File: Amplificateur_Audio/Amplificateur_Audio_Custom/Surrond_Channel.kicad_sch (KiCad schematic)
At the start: 84 parts, among them J401 Surrond Left+, J405 Analog input Connector, U401 PCM5252RHBR, U402 TPA3244DDWR, U403 74LVC1G125, U404 74LVC1G125

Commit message: Ajout de l'assignation des compostants et des empreintes jusqu'à la page 6
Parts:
- C401, C403, C405, C413, C415, C417, C419, C426, C427, C428, C429, C430, C431, C434, C435, C437, C439, C442, C443, C444, C445, C446: footprint (none) -> Capacitor_SMD:C_0603_1608Metric_Pad1.08x0.95mm_HandSolder
- C402, C404, C406, C407, C408, C409, C410, C411, C432, C433: footprint (none) -> Capacitor_SMD:C_0402_1005Metric_Pad0.74x0.62mm_HandSolder
- C412, C414, C416, C418, C420, C421, C422, C423, C424, C425: footprint (none) -> Capacitor_SMD:C_1206_3216Metric_Pad1.33x1.80mm_HandSolder
- C436, C438, C440, C441: footprint (none) -> Capacitor_SMD:C_1210_3225Metric_Pad1.33x2.70mm_HandSolder
- J401, J402, J403, J404: footprint (none) -> NewLibrary:630661MouserReel
- J405: footprint (none) -> Connector_PinHeader_2.54mm:PinHeader_2x25_P2.54mm_Vertical_SMD
- JP401, JP402, JP403, JP404: footprint (none) -> Connector_PinHeader_2.54mm:PinHeader_1x03_P2.54mm_Vertical_SMD_Pin1Left
- L401: footprint (none) -> Inductor_SMD:L_0603_1608Metric_Pad1.05x0.95mm_HandSolder
- L402, L403: footprint (none) -> NewLibrary:UA8014ALD
- R401, R402, R403, R404, R405, R406, R407: footprint (none) -> Resistor_SMD:R_0402_1005Metric_Pad0.72x0.64mm_HandSolder
- R408, R409, R410, R411, R412, R413, R414, R415, R416, R417, R419, R420, R421, R422: footprint (none) -> Resistor_SMD:R_0603_1608Metric_Pad0.98x0.95mm_HandSolder
- R418: footprint (none) -> Resistor_SMD:R_0201_0603Metric_Pad0.64x0.40mm_HandSolder
- U401: footprint (none) -> Package_DFN_QFN:Texas_RHB0032E_VQFN-32-1EP_5x5mm_P0.5mm_EP3.45x3.45mm_ThermalVias
- U403, U404: footprint (none) -> Package_TO_SOT_SMD:SOT-353_SC-70-5_Handsoldering
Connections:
- net 12V: now also C428.2; no longer C427.2
- net 3.3V-4: now also C403.2; no longer C405.2
- net GND: now also C430.2; no longer C430.1
- net VDD1: now also C427.2; no longer C428.2
- net at C404.2, R408.1, U401.14 (AVDD): now also C405.2; no longer C403.2
- net at U402.9 (AVDD): now also C430.1; no longer C430.2

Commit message: Ajout de point de test et début du routage
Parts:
- C422, C425: footprint Capacitor_SMD:C_1206_3216Metric_Pad1.33x1.80mm_HandSolder -> Capacitor_SMD:CP_Elec_16x17.5
- J402: value ~ -> Surrond Left-
- J403: value ~ -> Surrond Right+
- J404: value ~ -> SurroundRight-
- R418: footprint Resistor_SMD:R_0201_0603Metric_Pad0.64x0.40mm_HandSolder -> Resistor_SMD:R_0603_1608Metric_Pad0.98x0.95mm_HandSolder
- U402: footprint DDV0044D_N -> NewLibrary:DDV0044D_N
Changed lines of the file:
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@@
 	)
 	(symbol
+		(lib_id "Device:C_Polarized_Small_US")
+		(at 297.18 46.355 0)
+		(unit 1)
+		(exclude_from_sim no)
+		(in_bom yes)
+		(on_board yes)
+		(dnp no)
+		(fields_autoplaced yes)
+		(property "Reference" "C425"
+			(at 299.72 44.6531 0)
+			(effects
+				(font
+					(size 1.27 1.27)
+				)
+				(justify left)
+			)
+		)
+		(property "Value" "1000uF"
+			(at 299.72 47.1931 0)
+			(effects
+				(font
+					(size 1.27 1.27)
+				)
+				(justify left)
+			)
+		)
+		(property "Footprint" "Capacitor_SMD:CP_Elec_16x17.5"
+			(at 297.18 46.355 0)
+			(effects
+				(font
+					(size 1.27 1.27)
+				)
+				(hide yes)
+			)
+		)
+		(property "Datasheet" "~"
+			(at 297.18 46.355 0)
+			(effects
+				(font
+					(size 1.27 1.27)
+				)
+				(hide yes)
+			)
+		)
+		(property "Description" "EEV-FK1H102M"
+			(at 297.18 46.355 0)
+			(effects
+				(font
+					(size 1.27 1.27)
+				)
+				(hide yes)
+			)
+		)
+		(pin "1"
+		)
+		(pin "2"
+		)
+		(instances
+			(project "Amplificateur_Audio"
+				(path "/bf9cc67f-178f-4c8c-b6a6-249a1896d599/2266f535-6438-4aa9-912a-4ebf19d1b357"
+					(reference "C425")
+					(unit 1)
+				)
+			)
+		)
+	)
+	(symbol
 		(lib_id "Device:C_Small")
 		(at 262.89 178.435 90)
@@
 	)
 	(symbol
-		(lib_id "Device:C_Polarized_Small_US")
-		(at 297.18 46.355 0)
-		(unit 1)
-		(exclude_from_sim no)
-		(in_bom yes)
-		(on_board yes)
-		(dnp no)
-		(fields_autoplaced yes)
-		(property "Reference" "C425"
-			(at 299.72 44.6531 0)
-			(effects
-				(font
-					(size 1.27 1.27)
-				)
-				(justify left)
-			)
-		)
-		(property "Value" "1000uF"
-			(at 299.72 47.1931 0)
-			(effects
-				(font
-					(size 1.27 1.27)
-				)
-				(justify left)
-			)
-		)
-		(property "Footprint" "Capacitor_SMD:C_1206_3216Metric_Pad1.33x1.80mm_HandSolder"
-			(at 297.18 46.355 0)
-			(effects
-				(font
-					(size 1.27 1.27)
-				)
-				(hide yes)
-			)
-		)
-		(property "Datasheet" "~"
-			(at 297.18 46.355 0)
-			(effects
-				(font
-					(size 1.27 1.27)
-				)
-				(hide yes)
-			)
-		)
-		(property "Description" "GRM31MR71H105KA88L"
-			(at 297.18 46.355 0)
-			(effects
-				(font
-					(size 1.27 1.27)
-				)
-				(hide yes)
-			)
-		)
-		(pin "1"
-		)
-		(pin "2"
-		)
-		(instances
-			(project "Amplificateur_Audio"
-				(path "/bf9cc67f-178f-4c8c-b6a6-249a1896d599/2266f535-6438-4aa9-912a-4ebf19d1b357"
-					(reference "C425")
-					(unit 1)
-				)
-			)
-		)
-	)
-	(symbol
 		(lib_id "Device:C_Small")
 		(at 31.75 41.275 180)
@@
 			)
 		)
-		(property "Footprint" "DDV0044D_N"
+		(property "Footprint" "NewLibrary:DDV0044D_N"
 			(at 295.91 135.255 0)
 			(effects
@@
 			)
 		)
-		(property "Value" "~"
+		(property "Value" "Surrond Right+"
 			(at 401.955 109.22 0)
 			(effects
@@
 					(size 1.27 1.27)
 				)
+				(hide yes)
 			)
 		)
@@
 			)
 		)
-		(property "Value" "~"
+		(property "Value" "SurroundRight-"
 			(at 402.59 130.81 0)
 			(effects
@@
 					(size 1.27 1.27)
 				)
+				(hide yes)
 			)
 		)
@@
 	)
 	(symbol
-		(lib_id "Device:C_Small")
-		(at 184.15 69.215 90)
-		(unit 1)
-		(exclude_from_sim no)
-		(in_bom yes)
-		(on_board no)
-		(dnp no)
-		(property "Reference" "C414"
-			(at 184.023 64.262 90)
-			(effects
-				(font
-					(size 1.27 1.27)
-				)
-			)
-		)
-		(property "Value" "10uF"
-			(at 184.404 65.913 90)
-			(effects
-				(font
-					(size 1.27 1.27)
-				)
-			)
-		)
-		(property "Footprint" "Capacitor_SMD:C_1206_3216Metric_Pad1.33x1.80mm_HandSolder"
-			(at 184.15 69.215 0)
-			(effects
-				(font
-					(size 1.27 1.27)
-				)
-				(hide yes)
-			)
-		)
-		(property "Datasheet" "~"
-			(at 184.15 69.215 0)
-			(effects
-				(font
-					(size 1.27 1.27)
-				)
-				(hide yes)
-			)
-		)
-		(property "Description" "GRM31CR71C106KAC7L"
-			(at 184.15 69.215 0)
-			(effects
-				(font
-					(size 1.27 1.27)
-				)
-				(hide yes)
-			)
-		)
-		(pin "2"
-		)
-		(pin "1"
-		)
-		(instances
-			(project "BarreDeSonTI"
-				(path "/bf9cc67f-178f-4c8c-b6a6-249a1896d599/2266f535-6438-4aa9-912a-4ebf19d1b357"
-					(reference "C414")
-					(unit 1)
-				)
-			)
-		)
-	)
-	(symbol
 		(lib_id "power:Earth")
 		(at 337.82 169.545 0)
@@
 			)
 		)
-		(property "Value" "~"
+		(property "Value" "Surrond Left-"
 			(at 401.955 86.36 0)
 			(effects
@@
 					(size 1.27 1.27)
 				)
+				(hide yes)
 			)
 		)
@@
 	(symbol
 		(lib_id "Device:C_Small")
+		(at 184.15 69.215 90)
+		(unit 1)
+		(exclude_from_sim no)
+		(in_bom yes)
+		(on_board yes)
+		(dnp no)
+		(property "Reference" "C414"
+			(at 184.023 64.262 90)
+			(effects
+				(font
+					(size 1.27 1.27)
+				)
+			)
+		)
+		(property "Value" "10uF"
+			(at 184.404 65.913 90)
+			(effects
+				(font
+					(size 1.27 1.27)
+				)
+			)
+		)
+		(property "Footprint" "Capacitor_SMD:C_1206_3216Metric_Pad1.33x1.80mm_HandSolder"
+			(at 184.15 69.215 0)
+			(effects
+				(font
+					(size 1.27 1.27)
+				)
+				(hide yes)
+			)
+		)
+		(property "Datasheet" "~"
+			(at 184.15 69.215 0)
+			(effects
+				(font
+					(size 1.27 1.27)
+				)
+				(hide yes)
+			)
+		)
+		(property "Description" "GRM31CR71C106KAC7L"
+			(at 184.15 69.215 0)
+			(effects
+				(font
+					(size 1.27 1.27)
+				)
+				(hide yes)
+			)
+		)
+		(pin "2"
+		)
+		(pin "1"
+		)
+		(instances
+			(project "Amplificateur_Audio"
+				(path "/bf9cc67f-178f-4c8c-b6a6-249a1896d599/2266f535-6438-4aa9-912a-4ebf19d1b357"
+					(reference "C414")
+					(unit 1)
+				)
+			)
+		)
+	)
+	(symbol
+		(lib_id "Device:C_Small")
 		(at 370.205 92.075 180)
 		(unit 1)
@@
 			)
 		)
-		(property "Footprint" "Resistor_SMD:R_0201_0603Metric_Pad0.64x0.40mm_HandSolder"
+		(property "Footprint" "Resistor_SMD:R_0603_1608Metric_Pad0.98x0.95mm_HandSolder"
 			(at 266.7 198.755 0)
 			(effects
@@
 			)
 		)
-		(property "Footprint" "Capacitor_SMD:C_1206_3216Metric_Pad1.33x1.80mm_HandSolder"
+		(property "Footprint" "Capacitor_SMD:CP_Elec_16x17.5"
 			(at 290.83 27.305 0)
 			(effects
@@
 			)
 		)
-		(property "Description" "GRM31MR71H105KA88L"
+		(property "Description" "EEV-FK1H102M"
 			(at 290.83 27.305 0)
 			(effects

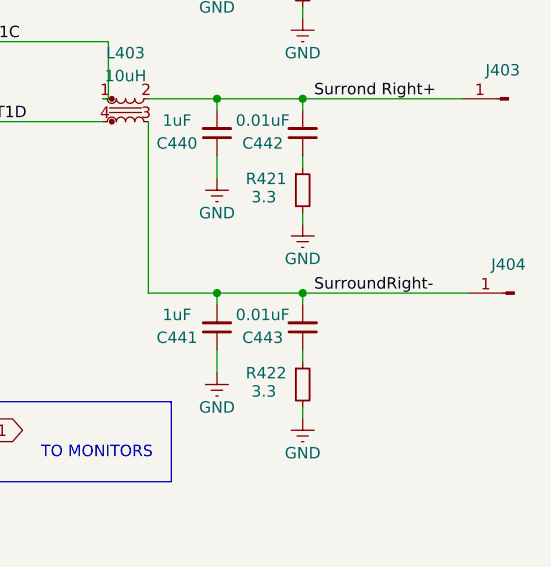
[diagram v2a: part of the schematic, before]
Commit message: Modification d'empreinte et routage de sortie audio
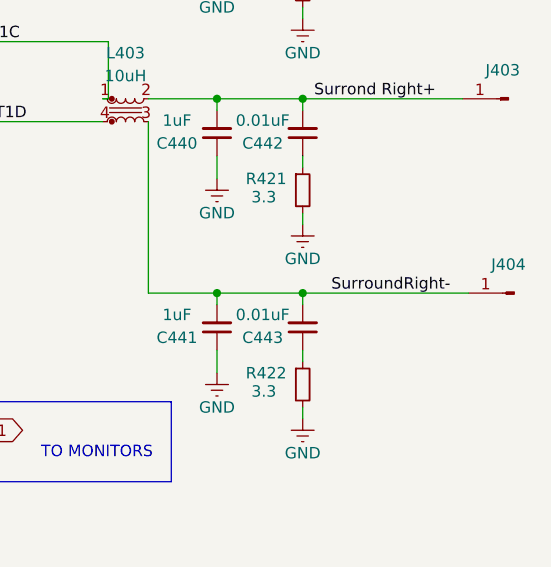
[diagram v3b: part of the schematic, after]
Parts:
- C422, C425: footprint Capacitor_SMD:CP_Elec_16x17.5 -> NewLibrary:CAP_EEVFK1H102M
- J401: value Surrond Left+ -> SL+
- J402: value Surrond Left- -> SL-
- J403: value Surrond Right+ -> SR+
- J404: value SurroundRight- -> SR-
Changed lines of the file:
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@@
 		)
 	)
+	(label "SurroundRight-"
+		(at 382.905 132.715 0)
+		(effects
+			(font
+				(size 1.27 1.27)
+			)
+			(justify left bottom)
+		)
+	)
 	(label "DAC1L-"
 		(at 162.56 59.055 0)
@@
 		)
 	)
-	(label "SurroundRight-"
-		(at 381 132.715 0)
-		(effects
-			(font
-				(size 1.27 1.27)
-			)
-			(justify left bottom)
-		)
-	)
 	(label "IND5"
 		(at 48.26 262.89 0)
@@
 			)
 		)
-		(property "Footprint" "Capacitor_SMD:CP_Elec_16x17.5"
+		(property "Footprint" "NewLibrary:CAP_EEVFK1H102M"
 			(at 297.18 46.355 0)
 			(effects
@@
 			)
 		)
-		(property "Value" "Surrond Right+"
+		(property "Value" "SR+"
 			(at 401.955 109.22 0)
 			(effects
@@
 			)
 		)
-		(property "Value" "Surrond Left+"
+		(property "Value" "SL+"
 			(at 401.955 64.77 0)
 			(effects
@@
 			)
 		)
-		(property "Value" "SurroundRight-"
+		(property "Value" "SR-"
 			(at 402.59 130.81 0)
 			(effects
@@
 			)
 		)
-		(property "Value" "Surrond Left-"
+		(property "Value" "SL-"
 			(at 401.955 86.36 0)
 			(effects
@@
 			)
 		)
-		(property "Footprint" "Capacitor_SMD:CP_Elec_16x17.5"
+		(property "Footprint" "NewLibrary:CAP_EEVFK1H102M"
 			(at 290.83 27.305 0)
 			(effects

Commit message: Continuation du routage
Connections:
- net OUT1A: now also L402.4; no longer L402.1
- net OUT1B: now also L402.1; no longer L402.4
- net OUT1C: now also L403.4; no longer L403.1
- net OUT1D: now also L403.1; no longer L403.4
- net Surrond Left+: now also L402.3; no longer L402.2
- net Surrond Left-: now also L402.2; no longer L402.3
- net Surrond Right+: now also L403.3; no longer L403.2
- net SurroundRight-: now also L403.2; no longer L403.3
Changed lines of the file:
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@@
 		(lib_id "Device:L_Iron_Coupled_Small_1243")
 		(at 360.045 67.945 0)
-		(unit 1)
-		(exclude_from_sim no)
-		(in_bom yes)
-		(on_board yes)
-		(dnp no)
-		(fields_autoplaced yes)
+		(mirror x)
+		(unit 1)
+		(exclude_from_sim no)
+		(in_bom yes)
+		(on_board yes)
+		(dnp no)
 		(property "Reference" "L402"
-			(at 360.045 61.595 0)
+			(at 360.045 74.295 0)
 			(effects
 				(font
@@
 		)
 		(property "Value" "10uH"
-			(at 360.045 64.135 0)
+			(at 360.045 71.755 0)
 			(effects
 				(font
@@
 		(lib_id "Device:L_Iron_Coupled_Small_1243")
 		(at 360.045 112.395 0)
-		(unit 1)
-		(exclude_from_sim no)
-		(in_bom yes)
-		(on_board yes)
-		(dnp no)
-		(fields_autoplaced yes)
+		(mirror x)
+		(unit 1)
+		(exclude_from_sim no)
+		(in_bom yes)
+		(on_board yes)
+		(dnp no)
 		(property "Reference" "L403"
-			(at 360.045 106.045 0)
+			(at 360.045 118.745 0)
 			(effects
 				(font
@@
 		)
 		(property "Value" "10uH"
-			(at 360.045 108.585 0)
-			(effects
-				(font
+			(at 360.045 116.205 0)
+			(effects
+				(font

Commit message: suite du routage
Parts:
- U402: footprint NewLibrary:DDV0044D_N -> Package_SO:HTSSOP-44-1EP_6.1x14mm_P0.635mm_EP5.2x14mm_Mask4.31x8.26mm_ThermalVias
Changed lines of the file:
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@@
 			)
 		)
-		(property "Footprint" "NewLibrary:DDV0044D_N"
+		(property "Footprint" "Package_SO:HTSSOP-44-1EP_6.1x14mm_P0.635mm_EP5.2x14mm_Mask4.31x8.26mm_ThermalVias"
 			(at 295.91 135.255 0)
 			(effects

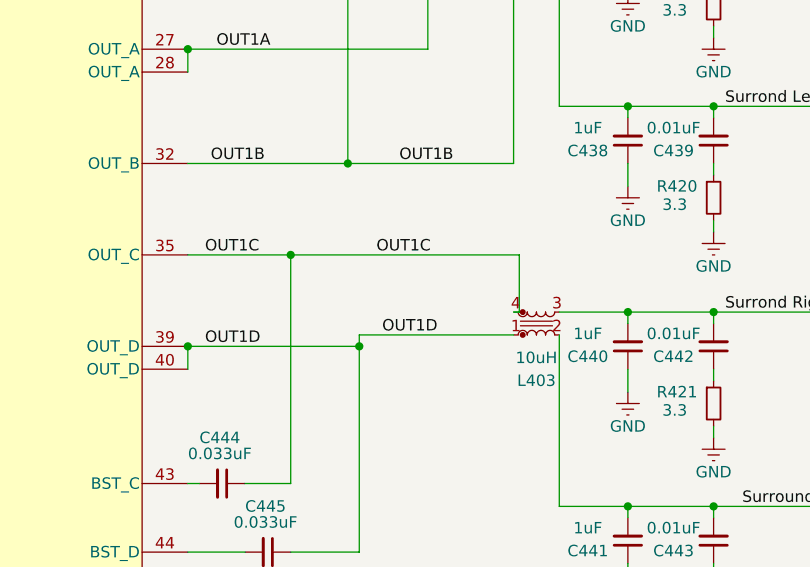
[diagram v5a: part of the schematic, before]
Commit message: Suite du routage passage des sorties d'ampli en symétrique et même longueur
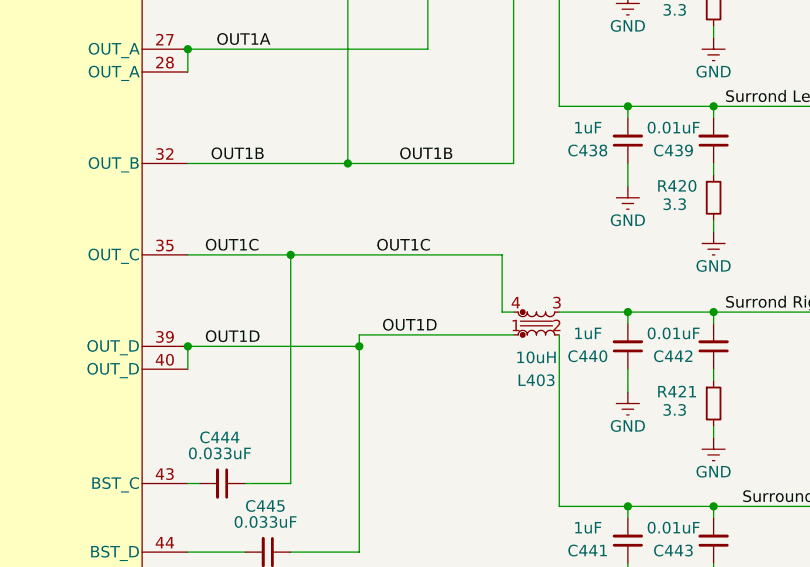
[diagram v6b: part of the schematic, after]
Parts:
- L402, L403: footprint NewLibrary:UA8014ALD -> NewLibrary:UA8014ALD_Reverse
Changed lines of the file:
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@@
 	(wire
 		(pts
-			(xy 358.14 111.125) (xy 357.505 111.125)
+			(xy 356.235 111.125) (xy 357.505 111.125)
 		)
 		(stroke
@@
 	(wire
 		(pts
-			(xy 358.14 104.775) (xy 358.14 111.125)
+			(xy 356.235 104.775) (xy 356.235 111.125)
 		)
 		(stroke
@@
 	(wire
 		(pts
-			(xy 332.74 104.775) (xy 358.14 104.775)
+			(xy 332.74 104.775) (xy 356.235 104.775)
 		)
 		(stroke
@@
 			)
 		)
-		(property "Footprint" "NewLibrary:UA8014ALD"
+		(property "Footprint" "NewLibrary:UA8014ALD_Reverse"
 			(at 360.045 67.945 0)
 			(effects
@@
 			)
 		)
-		(property "Footprint" "NewLibrary:UA8014ALD"
+		(property "Footprint" "NewLibrary:UA8014ALD_Reverse"
 			(at 360.045 112.395 0)
 			(effects
